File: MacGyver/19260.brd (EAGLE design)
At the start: 110.5 x 72.4 mm, 124 parts, among them J1 PST1,0/2-3,5, J10 RJ45J, J2 PPPC101LFBN, J3 PPPC101LFBN, J4 PPPC101LFBN, J5 Pi Zero, J6 PST1,0/3-3,5, J7 S04B, J9 RJ45J, Q1 IRFR5305, Q10 K38, Q101 K1N, Q102 K1N, Q103 K1N, Q11 K38, Q2 IRFR5305, Q3 P65, Q4 K3N, Q5 K1N, Q6 K3N, Q7 P65, Q8 K38, Q9 K1N, U1 1087, U101 Z4, U102 THVD1500, U103 Z4, U104 THVD1500, U105 THVD1500, U106 AVR128DB32-I/PT, U2 1087, U3 I50115, U4 I50115, U5 Z4, U6 AVR128DA28-I/SP, U7 Z4, Y1 16MHz

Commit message: MacGyver: layout wip
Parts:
- moved TP3 144.3 mm to (68.6, 62.2)
- moved C15 123.0 mm to (79.9, 32.5), turned to 270 degrees
- moved R19 120.5 mm to (71.2, 28.6), turned to 90 degrees
- moved R18 118.9 mm to (82.3, 28.7), turned to 90 degrees
- moved R22 118.6 mm to (82.3, 32.9), turned to 270 degrees
- moved R102 118.1 mm to (76.2, 64.8)
- moved R105 118.1 mm to (76.2, 61.0)
- moved R106 118.1 mm to (81.3, 61.0)
- moved R20 117.6 mm to (72.4, 39.4), turned to 90 degrees
- moved R21 116.8 mm to (76.2, 39.4), turned to 90 degrees
- moved C12 111.8 mm to (79.9, 29.2), turned to 90 degrees
- moved U5 104.8 mm to (76.7, 28.3), turned to 270 degrees
- moved U7 104.8 mm to (76.6, 33.3), turned to 270 degrees
- moved R17 101.1 mm to (68.6, 24.8)
- moved R103 86.4 mm to (54.4, 45.6)
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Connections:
- net ALT_EN: now also U106.1; no longer U106.15
- net APP_UART_: now also U106.24; no longer U106.32
- net APP_UPDI_: now also U106.25; no longer U106.1
- net PIPWR_EN: now also U106.32; no longer U106.16
- net RX_!RE: now also U106.15; no longer U106.2
- net RX_DE: now also U106.16; no longer U106.24
- net TX_!RE: now also U106.2; no longer U106.25
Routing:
- net MGR_LED: track 70.9 -> 0.00 mm, vias 3 -> 0
- net ALT_I: track 108.9 -> 49.7 mm, vias 3 -> 4
- net AIN0: track 0.00 -> 53.5 mm
- net AIN2: track 0.00 -> 51.7 mm
- net AIN1: track 0.00 -> 51.2 mm
- net N$93: track 48.0 -> 0.00 mm, vias 3 -> 0
- net AIN3: track 0.00 -> 47.7 mm
- net AIN5: track 0.00 -> 47.5 mm
- net AIN4: track 0.00 -> 45.4 mm
- net AIN6: track 0.00 -> 42.0 mm
- net ALT_V: track 130.4 -> 89.5 mm, vias 1 -> 6
- net AIN7: track 0.00 -> 39.8 mm
- net PWR_I: track 101.4 -> 62.5 mm, vias 1 -> 6
- net TX2: track 0.00 -> 32.5 mm
- net RX2: track 0.00 -> 29.7 mm
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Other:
- board size 110.5 x 72.4 mm -> 110.5 x 55.9 mm
- board text removed: "CS4"
- board text removed: "CS_ICP1"
- board text removed: "CS_ICP3"
- board text removed: "CS_ICP4"
- board text removed: "DIVERSION"
- board text removed: "FAST"
- board text removed: "ICP1"
- board text removed: "ICP3"
- board text removed: "ICP4"
- board text removed: "RX1"
- board text removed: "RX2"
- board text removed: "TX1"
- board text removed: "TX2"

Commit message: MacGyver: layout wip+
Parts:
- moved R120 20.2 mm to (41.9, 9.65)
- moved C105 14.7 mm to (39.2, 9.14), turned to 270 degrees
- moved U105 12.8 mm to (42.7, 13.6), turned to 90 degrees
- moved R119 10.6 mm to (54.9, 21.7), turned to 180 degrees
- moved Q103 8.87 mm to (51.4, 14.7)
- moved R121 8.14 mm to (47.8, 14.9), turned to 270 degrees
- moved R123 5.14 mm to (55.0, 18.3), turned to 270 degrees
- moved C15 4.58 mm to (83.7, 35.1)
- moved R22 4.02 mm to (86.1, 34.2)
- moved R122 2.54 mm to (45.7, 9.78)
- moved U7 1.27 mm to (76.6, 32.0)
- moved R116 0.99 mm to (19.7, 15.4)
- moved R128 0.13 mm to (17.1, 5.21)
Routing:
- net RX1: track 0.00 -> 58.8 mm, vias 0 -> 1
- net MGR_LED: track 0.00 -> 57.3 mm, vias 0 -> 1
- net SHUTDWN: track 0.00 -> 53.9 mm, vias 0 -> 3
- net TX1: track 0.00 -> 52.4 mm, vias 0 -> 1
- net +5V: track 284.7 -> 331.9 mm, vias 15 -> 13
- net !SS: track 0.00 -> 44.4 mm, vias 0 -> 1
- net PC3: track 0.00 -> 36.7 mm, vias 0 -> 2
- net PC2: track 0.00 -> 34.7 mm, vias 0 -> 2
- net I2C_SDA: track 0.00 -> 34.7 mm
- net MOSI: track 0.00 -> 34.3 mm
- net MISO: track 0.00 -> 34.2 mm
- net I2C_SCL: track 0.13 -> 34.3 mm
- net SCK: track 0.00 -> 33.9 mm
- net RX_!RE: track 0.00 -> 32.3 mm, vias 0 -> 2
- net FROM_RPU_RX: track 0.00 -> 27.0 mm, vias 0 -> 1
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
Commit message: MacGyver: layout wip++
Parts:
- removed TP2, TP3: TPPAD1-08, J-TP:P1-08
- moved R102 42.4 mm to (47.8, 33.3), turned to 270 degrees
- moved R105 25.2 mm to (83.4, 36.8), turned to 90 degrees
- moved R106 21.4 mm to (82.5, 39.6)
- moved R22 15.0 mm to (71.2, 32.1)
- moved R20 14.1 mm to (83.7, 31.0), turned to 180 degrees
- moved R127 13.4 mm to (87.1, 31.9), turned to 270 degrees
- moved R126 13.3 mm to (98.0, 30.6), turned to 270 degrees
- moved R125 12.1 mm to (92.6, 33.4), turned to 90 degrees
- moved R18 11.1 mm to (71.2, 28.4)
- moved C15 11.0 mm to (73.2, 32.0)
- moved R124 10.5 mm to (96.2, 34.2)
- moved TP1 9.04 mm to (80.1, 38.1)
- moved R21 8.35 mm to (79.9, 31.9), turned to 270 degrees
- moved R19 7.21 mm to (64.8, 25.4), turned to 270 degrees
- moved C12 6.75 mm to (73.2, 28.7)
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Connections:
- net N$1 renamed MGR_UPDI_PULLUP
- net N$3 renamed APP_UPDI_PULLUP
- net I2C_SCL: no longer TP2.TP
- net I2C_SDA: no longer TP1.TP
- net MGR_UPDI: now also TP1.TP; no longer TP3.TP
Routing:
- net PI_TX: track 0.00 -> 62.2 mm, vias 0 -> 4
- net PI_RX: track 0.00 -> 53.3 mm, vias 0 -> 5
- net I2C_SCL: track 34.3 -> 87.3 mm, vias 0 -> 2
- net FROM_RPU_TX: track 0.00 -> 52.7 mm, vias 0 -> 4
- net I2C_SDA: track 34.7 -> 85.6 mm, vias 0 -> 3
- net TO_RPU_RX: track 22.0 -> 72.2 mm, vias 1 -> 5
- net TO_RPU_TX: track 19.9 -> 56.4 mm, vias 2 -> 3
- net +5V: track 331.9 -> 365.9 mm, vias 13 -> 19
- net PI3V3: track 0.00 -> 30.4 mm, vias 0 -> 1
- net OOB_!RE: track 4.09 -> 28.4 mm, vias 0 -> 2
- net OOB_DE: track 0.00 -> 22.1 mm, vias 0 -> 2
- net FROM_RPU_OOB: track 1.47 -> 23.5 mm, vias 0 -> 1
- net TO_RPU_OOB: track 2.28 -> 23.6 mm, vias 0 -> 1
- net TX_DE: track 0.00 -> 20.2 mm, vias 0 -> 2
- net TX_!RE: track 8.30 -> 26.8 mm, vias 0 -> 2
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
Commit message: MacGyver: layout done, bom is next
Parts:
- moved R21 3.95 mm to (82.7, 29.1), turned to 180 degrees
- moved R19 1.99 mm to (66.5, 26.3), turned to 0 degrees
- moved R120 1.92 mm to (43.8, 9.40), turned to 270 degrees
- moved R17 1.45 mm to (65.7, 24.4), turned to 0 degrees
- moved C15 1.42 mm to (71.9, 31.4), turned to 180 degrees
- moved R22 1.28 mm to (71.1, 33.4), turned to 180 degrees
- moved U7 1.28 mm to (77.9, 32.8)
- moved U5 0.89 mm to (76.6, 27.7)
- moved Q103 0.74 mm to (50.8, 14.4), turned to 270 degrees
- moved C107 0.46 mm to (67.2, 38.7)
- moved R122 0.46 mm to (46.0, 9.40), turned to 90 degrees
- moved C12 0.13 mm to (73.2, 28.6)
- moved U105 0.13 mm to (42.7, 13.7)
- moved R127 0.13 mm to (87.2, 31.9)
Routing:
- net SHUTDWN: track 55.9 -> 115.0 mm, vias 3 -> 6
- net FROM_RPU_RX: track 27.0 -> 57.5 mm, vias 1 -> 5
- net I2C_SDA_: track 7.89 -> 36.8 mm, vias 0 -> 2
- net I2C_SCL_: track 4.46 -> 30.8 mm, vias 0 -> 2
- net APP_RX0: track 21.2 -> 46.6 mm, vias 0 -> 2
- net TO_RPU_TX: track 56.4 -> 77.2 mm, vias 3 -> 7
- net APP_TX0: track 21.0 -> 40.4 mm, vias 0 -> 2
- net MGR_UPDI: track 4.26 -> 21.8 mm, vias 0 -> 1
- net APP_UPDI_: track 0.00 -> 16.7 mm, vias 0 -> 2
- net FROM_RPU_OOB: track 23.5 -> 39.1 mm, vias 1 -> 2
- net TO_RPU_OOB: track 23.6 -> 37.4 mm, vias 1 -> 2
- net APP_UART_: track 0.00 -> 13.8 mm, vias 0 -> 2
- net APP_UPDI_PULLUP: track 0.00 -> 12.7 mm, vias 0 -> 2
- net APP_UPDI: track 48.5 -> 60.0 mm, vias 3 -> 5
- net +5V: track 365.9 -> 376.3 mm, vias 19 -> 20
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
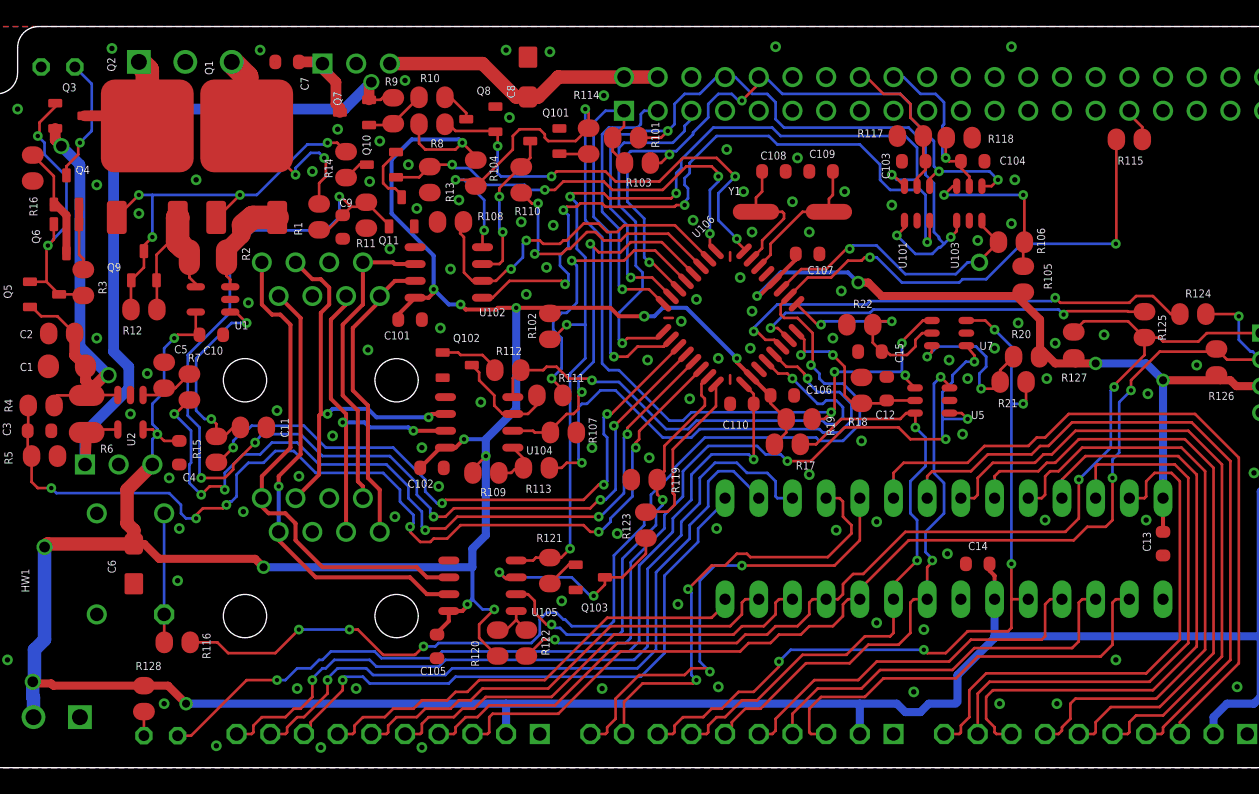
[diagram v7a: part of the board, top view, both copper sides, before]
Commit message: macgyver: layout done, needs reviewing
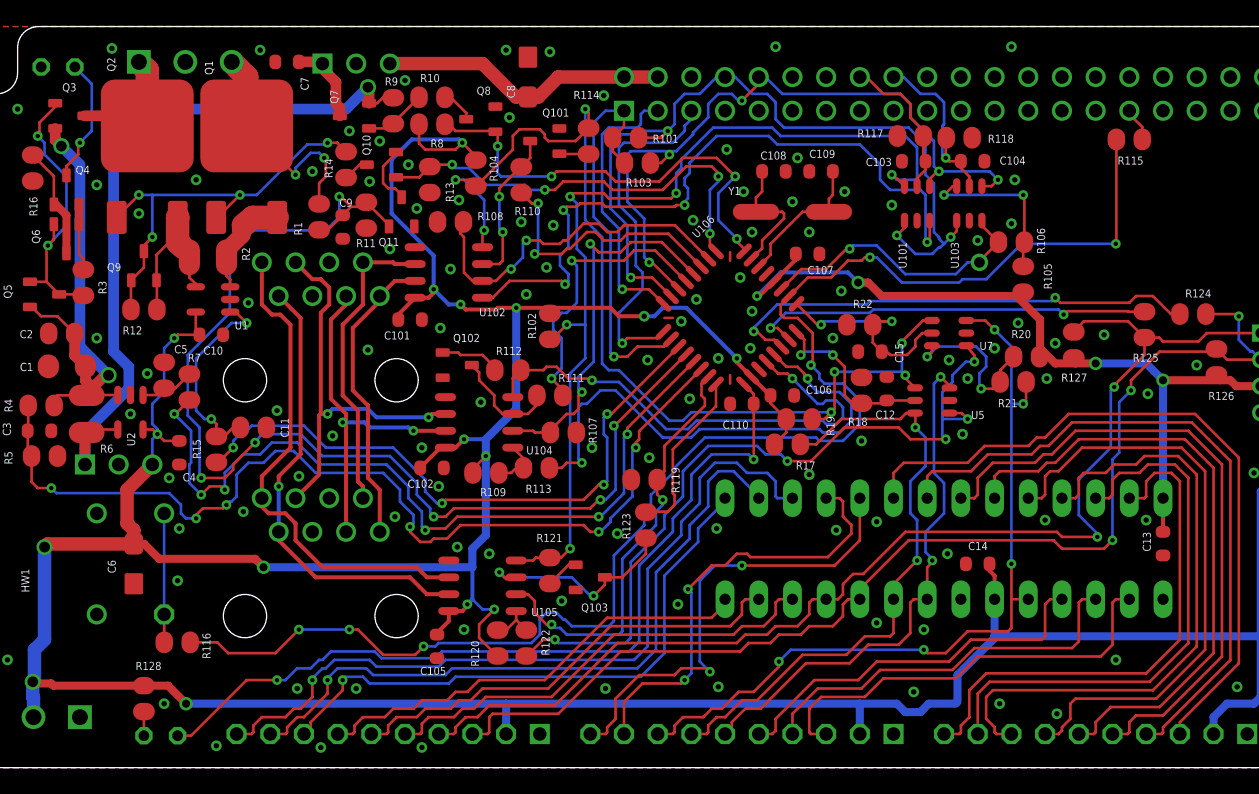
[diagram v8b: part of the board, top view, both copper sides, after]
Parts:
- moved Q7 0.25 mm to (33.0, 49.1)
- renumbered S201 to S101
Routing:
- net I2C_SCL: track 87.3 -> 90.4 mm
- net I2C_SDA: track 85.4 -> 86.8 mm
- net PC2: track 34.0 -> 33.2 mm
- net AIN6: track 42.8 -> 42.1 mm
- net +5V: track 376.3 -> 376.9 mm
- net 0V: vias 122 -> 125
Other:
- board text added: "!RESET"
- board text added: "!SS"
- board text added: "AIN2"
- board text added: "AIN3"
- board text added: "AIN4"
- board text added: "AIN5"
- board text added: "AIN6"
- board text added: "AIN7"
- board text added: "MISO"
- board text added: "MOSI"
- board text added: "PC2"
- board text added: "PC3"
- board text added: "RX0"
- board text added: "RX1"
- board text added: "RX2"
- board text added: "SCK"
- board text added: "TX0"
- board text added: "TX1"
- board text added: "TX2"
- board text added: "UPDI"
